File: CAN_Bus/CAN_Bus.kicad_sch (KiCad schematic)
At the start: 0 parts

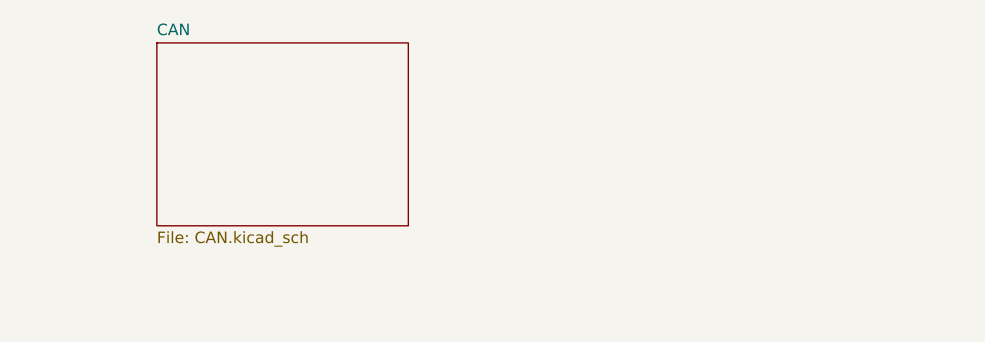
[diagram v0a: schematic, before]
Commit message: finalized schematic (not pcb)
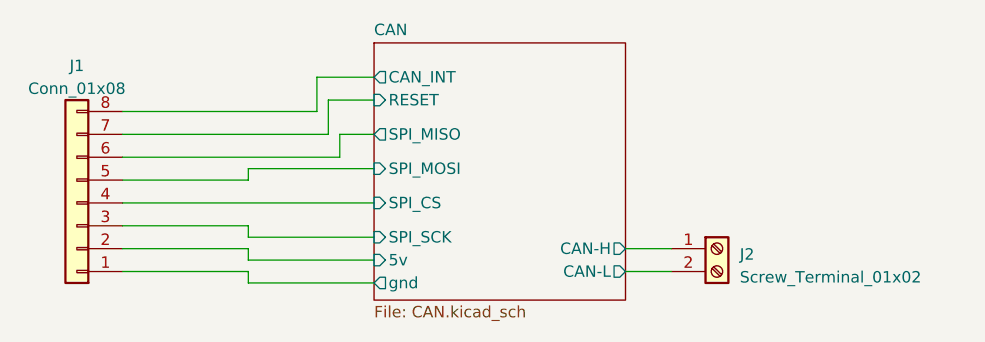
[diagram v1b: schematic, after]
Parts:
- added J1: Conn_01x08, Connector_PinHeader_2.54mm:PinHeader_1x08_P2.54mm_Horizontal, symbol Connector_Generic:Conn_01x08
- added J2: Screw_Terminal_01x02, TerminalBlock_Phoenix:TerminalBlock_Phoenix_MKDS-1,5-2_1x02_P5.00mm_Horizontal, symbol Connector:Screw_Terminal_01x02
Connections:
- new net CAN/5v: J1.2 (Pin_2)
- new net CAN/CAN-H: J2.1 (Pin_1)
- new net CAN/CAN-L: J2.2 (Pin_2)
- new net CAN/CAN_INT: J1.8 (Pin_8)
- new net CAN/RESET: J1.7 (Pin_7)
- new net CAN/SPI_CS: J1.4 (Pin_4)
- new net CAN/SPI_MISO: J1.6 (Pin_6)
- new net CAN/SPI_MOSI: J1.5 (Pin_5)
- new net CAN/SPI_SCK: J1.3 (Pin_3)
- new net CAN/gnd: J1.1 (Pin_1)
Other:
- sheet CAN ports: added 5v, CAN-H, CAN-L, CAN_INT, RESET, SPI_CS, SPI_MISO, SPI_MOSI, SPI_SCK, gnd; removed none
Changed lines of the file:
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@@
 (kicad_sch (version 20230121) (generator eeschema)
   (paper "A4")
-  (sheet (at 110.49 83.82) (size 27.94 20.32) (fields_autoplaced)
+  (wire (pts (xy 134.62 107.95) (xy 120.65 107.95))
+    (stroke (width 0) (type default))
+  )
+  (wire (pts (xy 120.65 110.49) (xy 134.62 110.49))
+    (stroke (width 0) (type default))
+  )
+  (wire (pts (xy 106.68 96.52) (xy 130.81 96.52))
+    (stroke (width 0) (type default))
+  )
+  (wire (pts (xy 162.56 106.68) (xy 167.64 106.68))
+    (stroke (width 0) (type default))
+  )
+  (wire (pts (xy 120.65 106.68) (xy 106.68 106.68))
+    (stroke (width 0) (type default))
+  )
+  (wire (pts (xy 130.81 96.52) (xy 130.81 93.98))
+    (stroke (width 0) (type default))
+  )
+  (wire (pts (xy 120.65 99.06) (xy 120.65 97.79))
+    (stroke (width 0) (type default))
+  )
+  (wire (pts (xy 120.65 99.06) (xy 106.68 99.06))
+    (stroke (width 0) (type default))
+  )
+  (wire (pts (xy 106.68 109.22) (xy 120.65 109.22))
+    (stroke (width 0) (type default))
+  )
+  (wire (pts (xy 120.65 109.22) (xy 120.65 110.49))
+    (stroke (width 0) (type default))
+  )
+  (wire (pts (xy 128.27 91.44) (xy 128.27 87.63))
+    (stroke (width 0) (type default))
+  )
+  (wire (pts (xy 120.65 104.14) (xy 120.65 105.41))
+    (stroke (width 0) (type default))
+  )
+  (wire (pts (xy 130.81 93.98) (xy 134.62 93.98))
+    (stroke (width 0) (type default))
+  )
+  (wire (pts (xy 106.68 104.14) (xy 120.65 104.14))
+    (stroke (width 0) (type default))
+  )
+  (wire (pts (xy 134.62 97.79) (xy 120.65 97.79))
+    (stroke (width 0) (type default))
+  )
+  (wire (pts (xy 120.65 105.41) (xy 134.62 105.41))
+    (stroke (width 0) (type default))
+  )
+  (wire (pts (xy 120.65 106.68) (xy 120.65 107.95))
+    (stroke (width 0) (type default))
+  )
+  (wire (pts (xy 128.27 87.63) (xy 134.62 87.63))
+    (stroke (width 0) (type default))
+  )
+  (wire (pts (xy 134.62 90.17) (xy 129.54 90.17))
+    (stroke (width 0) (type default))
+  )
+  (wire (pts (xy 106.68 91.44) (xy 128.27 91.44))
+    (stroke (width 0) (type default))
+  )
+  (wire (pts (xy 162.56 109.22) (xy 167.64 109.22))
+    (stroke (width 0) (type default))
+  )
+  (wire (pts (xy 106.68 101.6) (xy 134.62 101.6))
+    (stroke (width 0) (type default))
+  )
+  (wire (pts (xy 129.54 93.98) (xy 106.68 93.98))
+    (stroke (width 0) (type default))
+  )
+  (wire (pts (xy 129.54 93.98) (xy 129.54 90.17))
+    (stroke (width 0) (type default))
+  )
+  (symbol (lib_id "Connector:Screw_Terminal_01x02") (at 172.72 106.68 0) (unit 1)
+    (in_bom yes) (on_board yes) (dnp no) (fields_autoplaced)
+    (property "Reference" "J2" (at 175.26 107.315 0)
+      (effects (font (size 1.27 1.27)) (justify left))
+    )
+    (property "Value" "Screw_Terminal_01x02" (at 175.26 109.855 0)
+      (effects (font (size 1.27 1.27)) (justify left))
+    )
+    (property "Footprint" "TerminalBlock_Phoenix:TerminalBlock_Phoenix_MKDS-1,5-2_1x02_P5.00mm_Horizontal" (at 172.72 106.68 0)
+      (effects (font (size 1.27 1.27)) hide)
+    )
+    (property "Datasheet" "~" (at 172.72 106.68 0)
+      (effects (font (size 1.27 1.27)) hide)
+    )
+    (pin "1")
+    (pin "2")
+    (instances
+      (project "CAN_Bus"
+        (path "/f948908f-a766-40c4-8fbf-8f39d474d206"
+          (reference "J2") (unit 1)
+        )
+      )
+    )
+  )
+  (symbol (lib_id "Connector_Generic:Conn_01x08") (at 101.6 101.6 180) (unit 1)
+    (in_bom yes) (on_board yes) (dnp no) (fields_autoplaced)
+    (property "Reference" "J1" (at 101.6 86.36 0)
+      (effects (font (size 1.27 1.27)))
+    )
+    (property "Value" "Conn_01x08" (at 101.6 88.9 0)
+      (effects (font (size 1.27 1.27)))
+    )
+    (property "Footprint" "Connector_PinHeader_2.54mm:PinHeader_1x08_P2.54mm_Horizontal" (at 101.6 101.6 0)
+      (effects (font (size 1.27 1.27)) hide)
+    )
+    (property "Datasheet" "~" (at 101.6 101.6 0)
+      (effects (font (size 1.27 1.27)) hide)
+    )
+    (pin "1")
+    (pin "2")
+    (pin "3")
+    (pin "4")
+    (pin "5")
+    (pin "6")
+    (pin "7")
+    (pin "8")
+    (instances
+      (project "CAN_Bus"
+        (path "/f948908f-a766-40c4-8fbf-8f39d474d206"
+          (reference "J1") (unit 1)
+        )
+      )
+    )
+  )
+  (sheet (at 134.62 83.82) (size 27.94 28.575) (fields_autoplaced)
     (stroke (width 0.1524) (type solid))
     (fill (color 0 0 0 0.0000))
-    (property "Sheetname" "CAN" (at 110.49 83.1084 0)
+    (property "Sheetname" "CAN" (at 134.62 83.1084 0)
       (effects (font (size 1.27 1.27)) (justify left bottom))
     )
-    (property "Sheetfile" "CAN.kicad_sch" (at 110.49 104.7246 0)
+    (property "Sheetfile" "CAN.kicad_sch" (at 134.62 112.9796 0)
       (effects (font (size 1.27 1.27)) (justify left top))
     )
+    (pin "CAN_INT" output (at 134.62 87.63 180)
+      (effects (font (size 1.27 1.27)) (justify left))
+    )
+    (pin "CAN-H" output (at 162.56 106.68 0)
+      (effects (font (size 1.27 1.27)) (justify right))
+    )
+    (pin "RESET" input (at 134.62 90.17 180)
+      (effects (font (size 1.27 1.27)) (justify left))
+    )
+    (pin "CAN-L" output (at 162.56 109.22 0)
+      (effects (font (size 1.27 1.27)) (justify right))
+    )
+    (pin "SPI_MISO" output (at 134.62 93.98 180)
+      (effects (font (size 1.27 1.27)) (justify left))
+    )
+    (pin "SPI_MOSI" input (at 134.62 97.79 180)
+      (effects (font (size 1.27 1.27)) (justify left))
+    )
+    (pin "SPI_SCK" input (at 134.62 105.41 180)
+      (effects (font (size 1.27 1.27)) (justify left))
+    )
+    (pin "SPI_CS" input (at 134.62 101.6 180)
+      (effects (font (size 1.27 1.27)) (justify left))
+    )
+    (pin "5v" input (at 134.62 107.95 180)
+      (effects (font (size 1.27 1.27)) (justify left))
+    )
+    (pin "gnd" output (at 134.62 110.49 180)
+      (effects (font (size 1.27 1.27)) (justify left))
+    )
     (instances
